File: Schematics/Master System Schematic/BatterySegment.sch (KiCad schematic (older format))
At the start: 148 parts

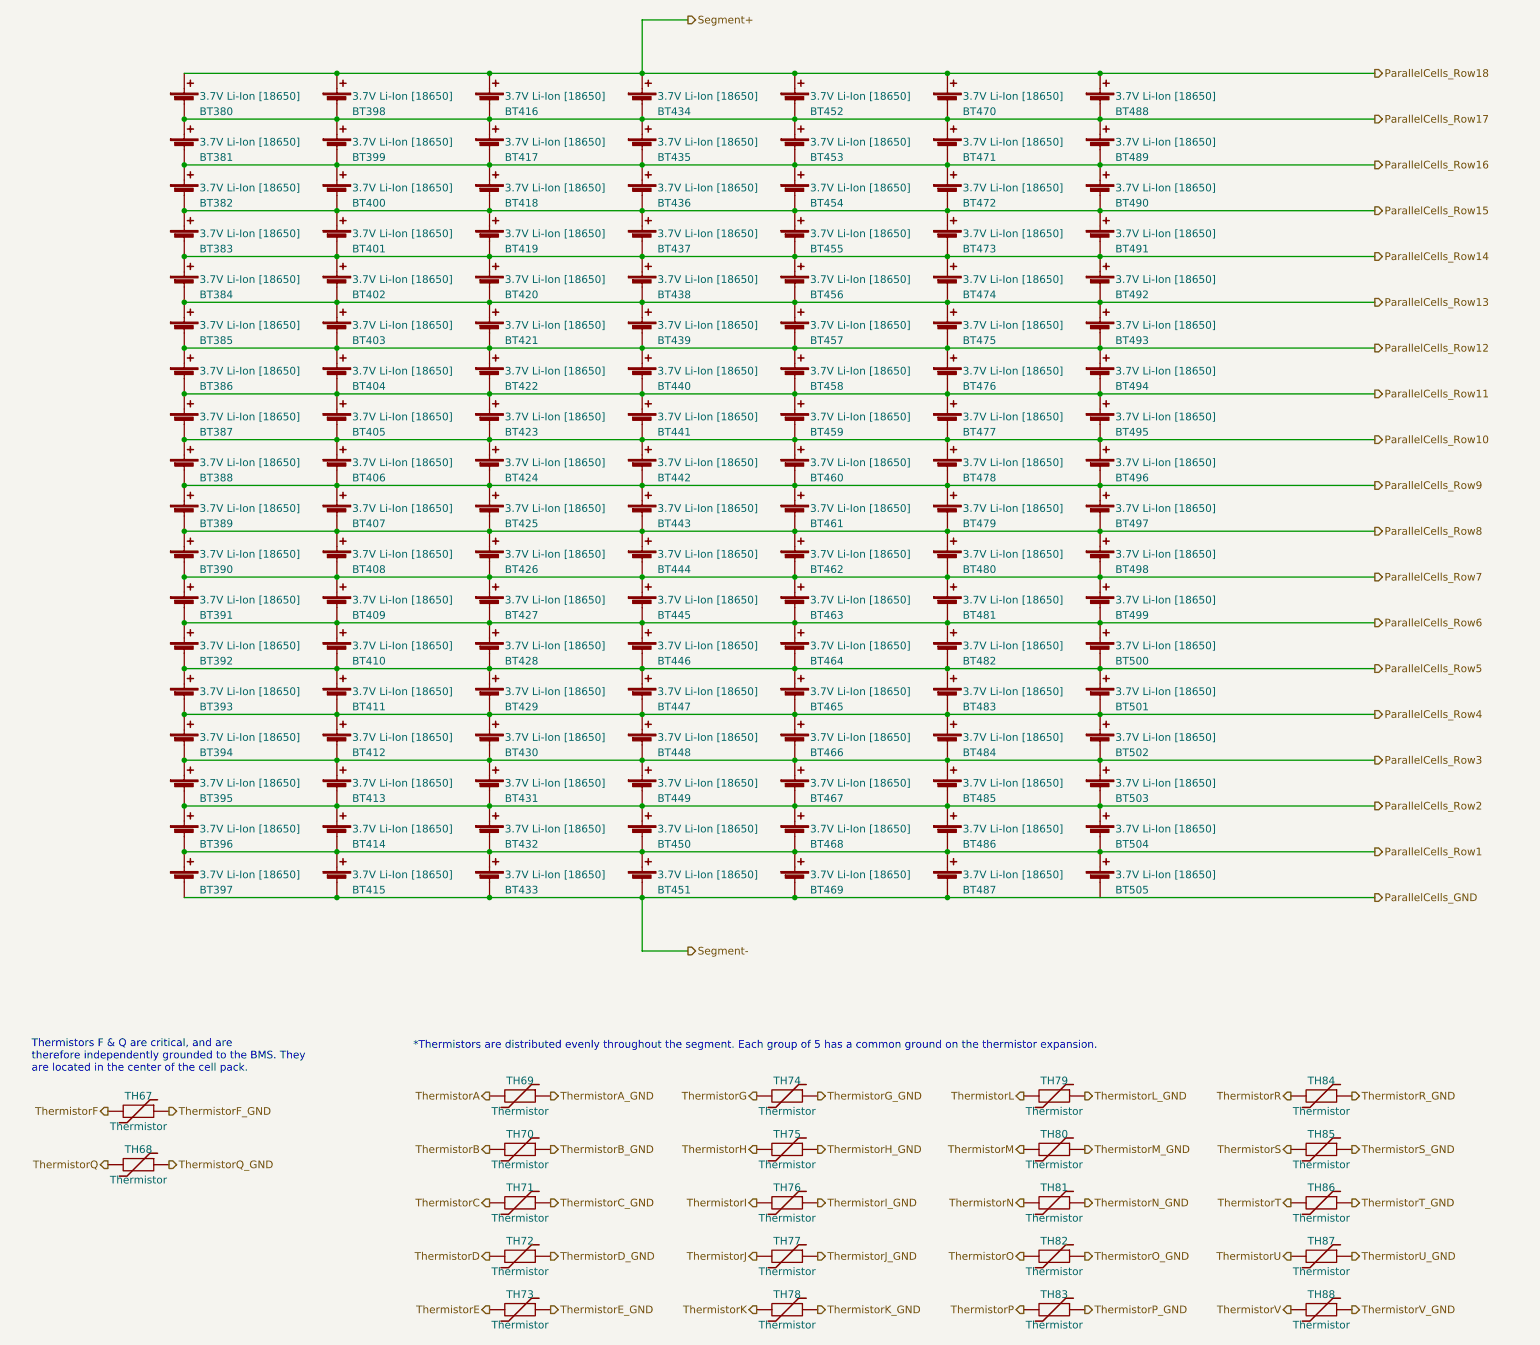
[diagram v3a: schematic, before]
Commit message: Segment Layer
> Added segments to Segment_Layer sheet
> Added VT PCBs and Thermistor PCBs to Segment_Layer sheet
> Removed relays from VT PCBs
> Still need to add connectors to VT and Thermistor PCBs once PCBs have been redesigned
> Added outputs for Segment_Layer sheet
> Added wire gauges to Segment_Layer sheet

Segment_Layer V1.0
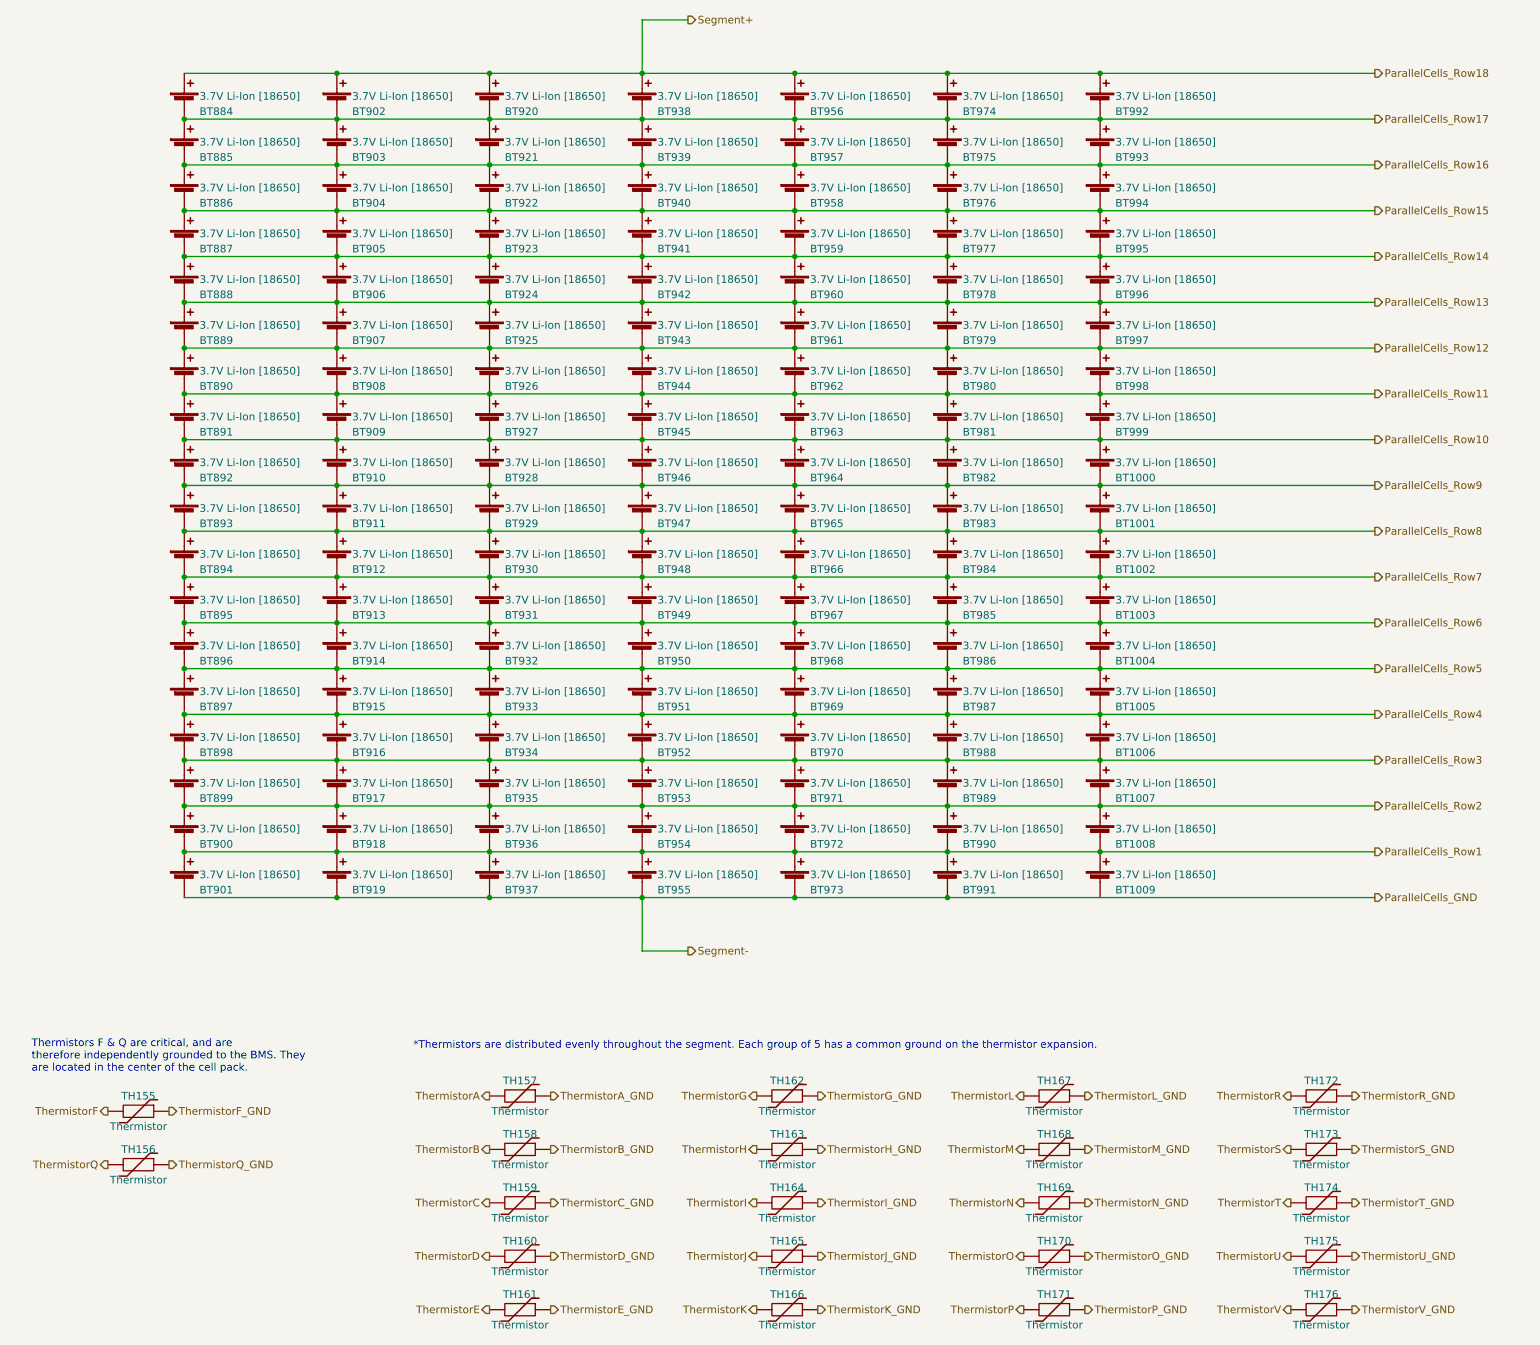
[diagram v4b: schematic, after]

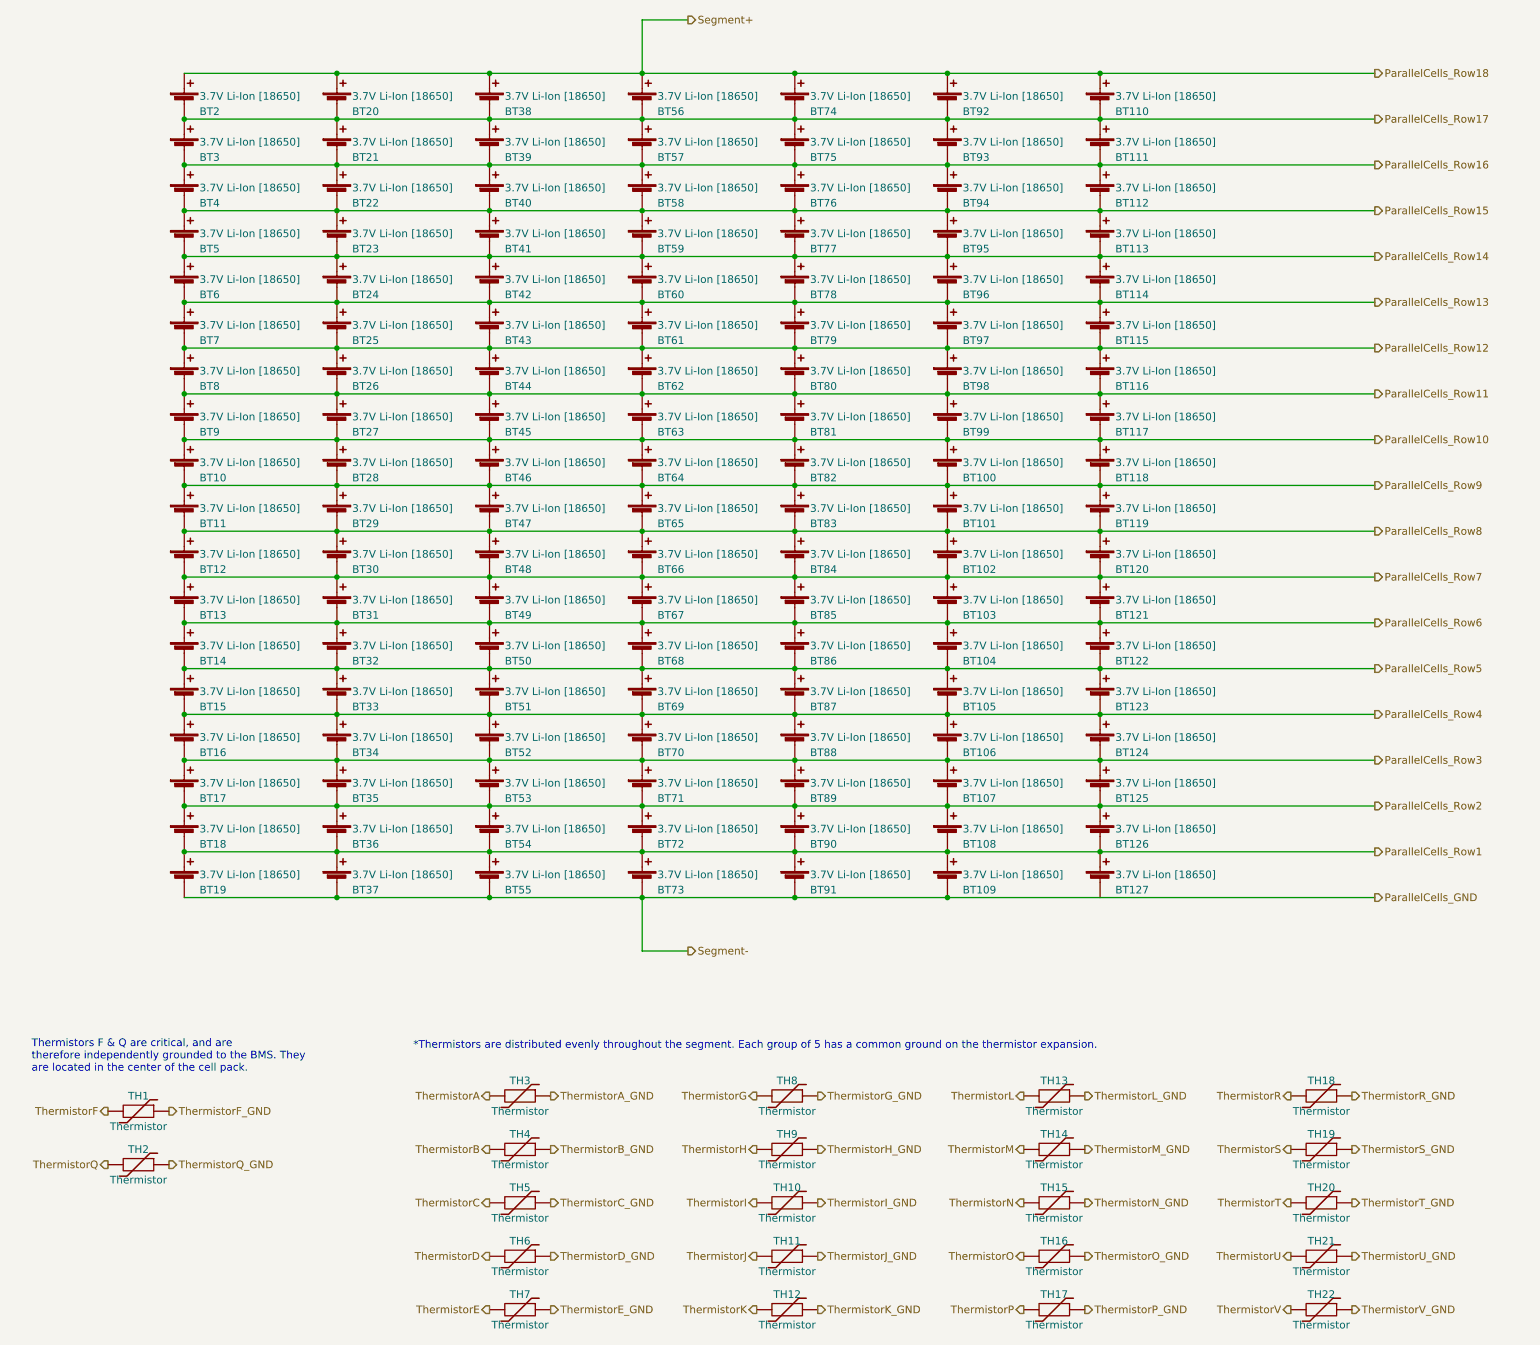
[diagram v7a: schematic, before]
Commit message: Battery Box KiCAD Update (#103)
* LV Plate and VPM board

Verified and updated LV plate connections
Setup VPM board stand-in
Organized main battery box schematic

* Battbox and master update

- Fixed all connections within battbox and did some formatting
- Added all battbox connections to master

* Annotations complete

* VPM callout

Added call to view altium schematic for VPM boarrd

* TSAL call out

Redirect to altium for TSAL

* Dates and stuff

- Final annotations
- Updated title blocks

* Exported

Plotted full file

Co-authored-by: Zack Perry <zperry2002@gmail.com>
Co-authored-by: Zack Perry <60787475+ziptol@users.noreply.github.com>
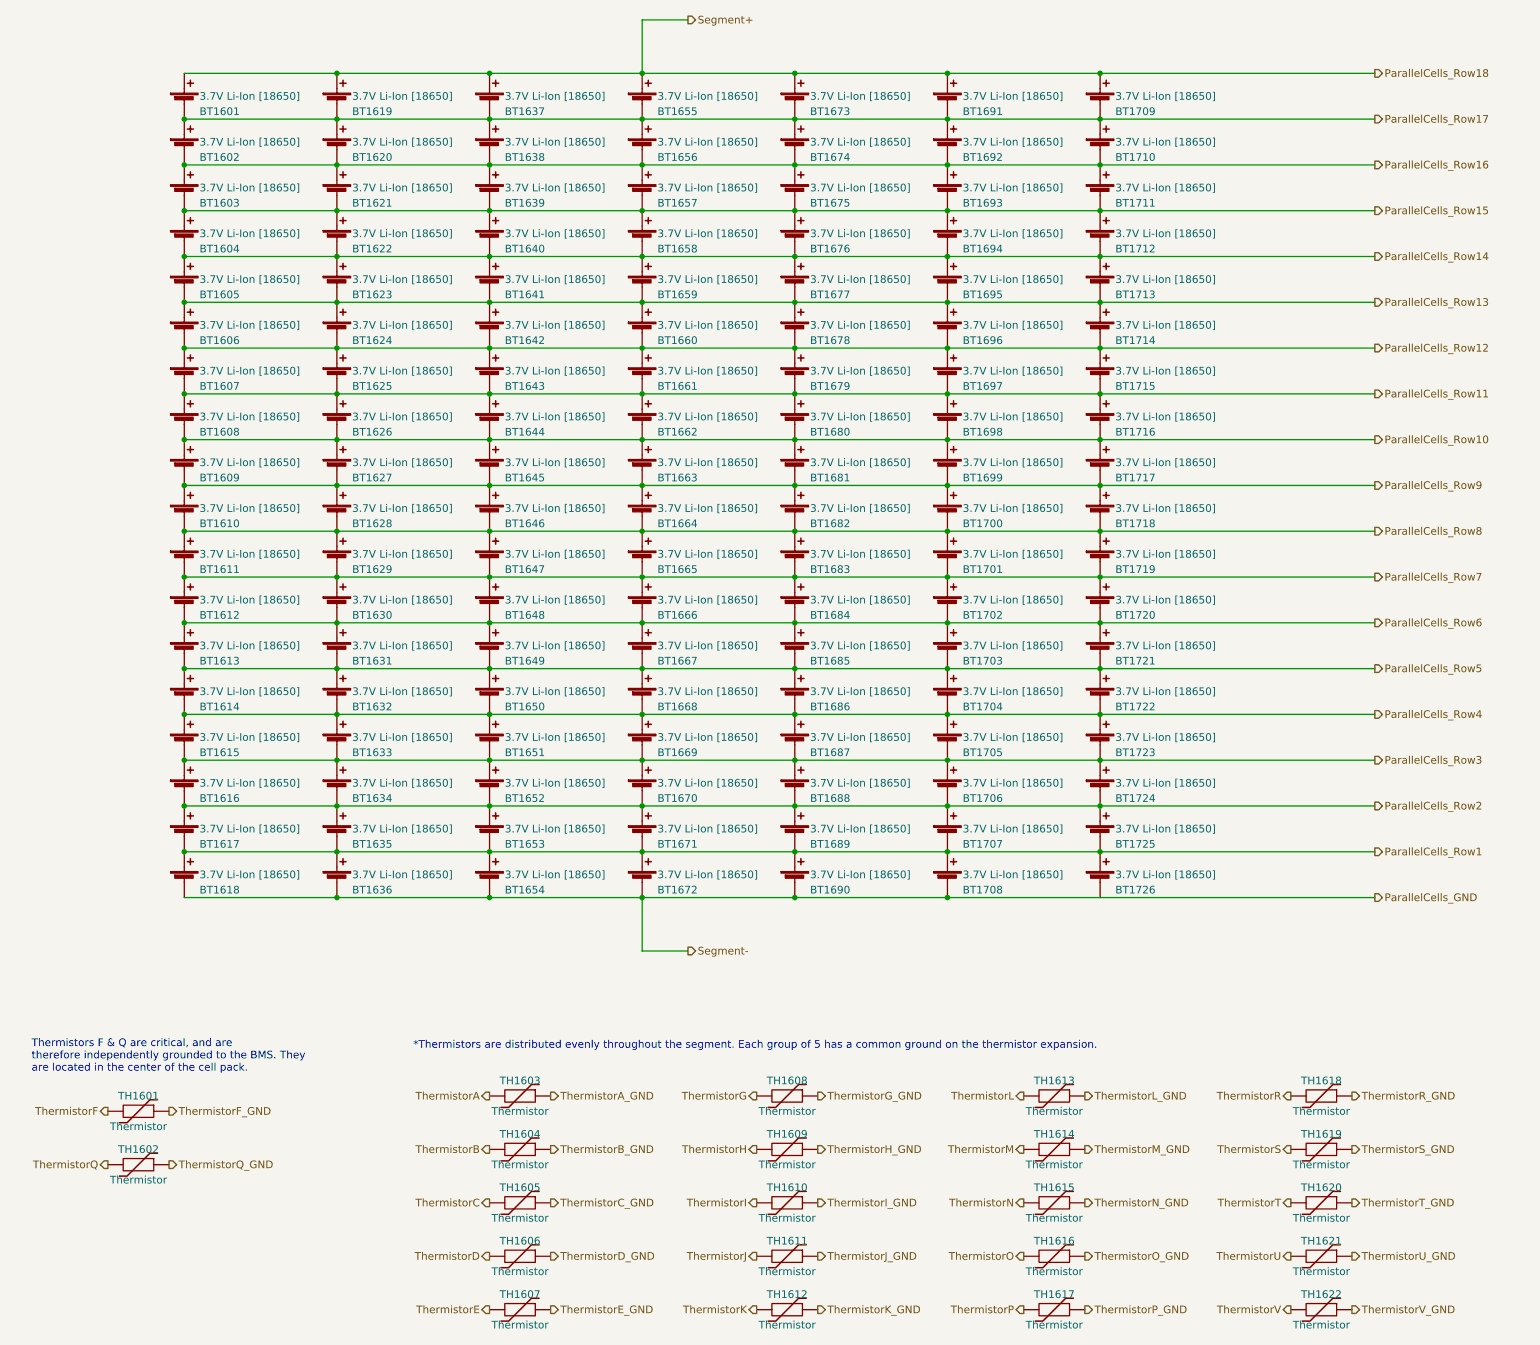
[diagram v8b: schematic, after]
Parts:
- renumbered BT2 to BT1001, BT3 to BT1002, BT4 to BT1003, BT5 to BT1004, BT6 to BT1005, BT7 to BT1006, BT8 to BT1007, BT9 to BT1008, BT10 to BT1009, BT11 to BT1010, BT12 to BT1011, BT13 to BT1012, BT14 to BT1013, BT15 to BT1014, BT16 to BT1015, BT17 to BT1016, BT18 to BT1017, BT19 to BT1018, BT20 to BT1019, BT21 to BT1020, BT22 to BT1021, BT23 to BT1022, BT24 to BT1023, BT25 to BT1024, BT26 to BT1025, BT27 to BT1026, BT28 to BT1027, BT29 to BT1028, BT30 to BT1029, BT31 to BT1030, BT32 to BT1031, BT33 to BT1032, BT34 to BT1033, BT35 to BT1034, BT36 to BT1035, BT37 to BT1036, BT38 to BT1037, BT39 to BT1038, BT40 to BT1039, BT41 to BT1040, BT42 to BT1041, BT43 to BT1042, BT44 to BT1043, BT45 to BT1044, BT46 to BT1045, BT47 to BT1046, BT48 to BT1047, BT49 to BT1048, BT50 to BT1049, BT51 to BT1050, BT52 to BT1051, BT53 to BT1052, BT54 to BT1053, BT55 to BT1054, BT56 to BT1055, BT57 to BT1056, BT58 to BT1057, BT59 to BT1058, BT60 to BT1059, BT61 to BT1060, BT62 to BT1061, BT63 to BT1062, BT64 to BT1063, BT65 to BT1064, BT66 to BT1065, BT67 to BT1066, BT68 to BT1067, BT69 to BT1068, BT70 to BT1069, BT71 to BT1070, BT72 to BT1071, BT73 to BT1072, BT74 to BT1073, BT75 to BT1074, BT76 to BT1075, BT77 to BT1076, BT78 to BT1077, BT79 to BT1078, BT80 to BT1079, BT81 to BT1080, BT82 to BT1081, BT83 to BT1082, BT84 to BT1083, BT85 to BT1084, BT86 to BT1085, BT87 to BT1086, BT88 to BT1087, BT89 to BT1088, BT90 to BT1089, BT91 to BT1090, BT92 to BT1091, BT93 to BT1092, BT94 to BT1093, BT95 to BT1094, BT96 to BT1095, BT97 to BT1096, BT98 to BT1097, BT99 to BT1098, BT100 to BT1099, BT101 to BT1100, BT102 to BT1101, BT103 to BT1102, BT104 to BT1103, BT105 to BT1104, BT106 to BT1105, BT107 to BT1106, BT108 to BT1107, BT109 to BT1108, BT110 to BT1109, BT111 to BT1110, BT112 to BT1111, BT113 to BT1112, BT114 to BT1113, BT115 to BT1114, BT116 to BT1115, BT117 to BT1116, BT118 to BT1117, BT119 to BT1118, BT120 to BT1119, BT121 to BT1120, BT122 to BT1121, BT123 to BT1122, BT124 to BT1123, BT125 to BT1124, BT126 to BT1125, BT127 to BT1126, TH1 to TH1001, TH2 to TH1002, TH3 to TH1003, TH4 to TH1004, TH5 to TH1005, TH6 to TH1006, TH7 to TH1007, TH8 to TH1008, TH9 to TH1009, TH10 to TH1010, TH11 to TH1011, TH12 to TH1012, TH13 to TH1013, TH14 to TH1014, TH15 to TH1015, TH16 to TH1016, TH17 to TH1017, TH18 to TH1018, TH19 to TH1019, TH20 to TH1020, TH21 to TH1021, TH22 to TH1022
